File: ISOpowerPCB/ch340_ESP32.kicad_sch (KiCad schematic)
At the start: 8 parts

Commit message: significant changes
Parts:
- added SW?: EN, symbol 000_Switches_Immo:pushbutton_tactile_2pin_SMD
- added SW?: BOOT, symbol 000_Switches_Immo:pushbutton_tactile_2pin_SMD
- R? (x2): value Resistor_0805 -> 10k
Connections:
- net ESP_EN: now also SW?.1
- net ESP_IO0: now also SW?.1
- net GND: now also SW?.2, SW?.2
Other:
- note removed: "USB power routed to its own bus, to allow potential for USB power to be used for powering microcontrollers during programming, but avoid case where user inadvertently tries to power entire 5v BUS from USB rail"
- moved on the sheet: C?, J?, Q?, R?, U?

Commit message: Updated as per discussions 26/01/22
# Change Notes

04/02/2022
As per discussion 26/01/22
1. Changed per channel 5v MOSFET switches to MOSFET control of DC/DC module on/off pin - due to failure of MOSFET switching during testing.
2. Added 5v buck converter for independent MCU_5V power bus.
	- Ensured all 5v MCU hardware is powered from common MCU_5V bus.
3. Removed circuit from NC pins on DC/DC modules.
4. Changed ESP32 USB interface to CH340
5. Changed MCU serial logic level converters from MOSFET to IC - TXS0102DCT
	- TODO: OE pin now requires low signal untill DC/DC supply is stable - Does it? Can it just be tied to 5v bus with a large capacitor? Does it need MCU to hold pin low untill 5V_BUS is stable?
6. Removed redundent 3V3_IN to power distribution page.
	- Rechecked all sheets for redundent pins, it won't impact drawing traces, but it will impact readability.
7. Added Mechanical layer as hirarchical sheet.
8. Moved voltage monitoring circuits to hirarchical sheet
9. Added voltage monitoring with TL431DBZ to 12V_BUS
10. Automatic shutoff circuit removed, as this would prevent the DC/DC module from powering on. Instead moved to AtMega328p digital inputs
and microcontroller will control shutdown of DC/DC supply if out of spec voltage detected.
		- This is a severe limitation compared to the specification, and this also does not prevent damage to devices on 5V_BUS if voltage is pulled high, for example to 12v due to user error.
		- TODO: Add independent overvoltage protection to 5V_BUS? 		[Zener Diode Overvoltage Protection - Sparkfun](https://www.rs-online.com/designspark/how-does-zener-diode-do-overvoltage-protection-in-circuit#:~:text=In%20order%20to%20protect%20the,flow%20in%20the%20reverse%20direction).
11. Changed logic level conversion for 12v outputs to 12v drive circuit. [12v drive circuit](https://forum.arduino.cc/t/easiest-way-of-driving-amplifying-from-5v-to-12v/123290)
12. Added proto pin connections for ESP MCU.
13. Changed 20v Zener in reverse vol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
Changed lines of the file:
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@@
     (effects (font (size 1.27 1.27)) (justify left))
   )
-  (hierarchical_label "GND" (shape bidirectional) (at 25.4 24.13 180)
+  (hierarchical_label "GND" (shape passive) (at 25.4 24.13 180)
     (effects (font (size 1.27 1.27)) (justify right))
   )

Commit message: messing around with libraries
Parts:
- C28, C29: renamed from C?; symbol 000_Capacitor_film_immo:cap_film_0805 -> 000_Capacitor_FIlm_Immo:cap_film_0805
- gave numbers to parts that had none: 8
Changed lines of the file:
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@@
     (effects (font (size 1.27 1.27)) (justify left))
   )
-  (symbol (lib_id "000_Capacitor_film_immo:cap_film_0805") (at 127 66.04 270) (mirror x) (unit 1)
-    (in_bom yes) (on_board yes)
-    (property "Reference" "C?" (id 0) (at 129.54 64.77 90))
+  (symbol (lib_id "000_Capacitor_FIlm_Immo:cap_film_0805") (at 127 66.04 270) (mirror x) (unit 1)
+    (in_bom yes) (on_board yes)
+    (property "Reference" "C28" (id 0) (at 129.54 64.77 90))
     (property "Value" "100n" (id 1) (at 123.19 64.77 90))
     (property "Footprint" "Capacitor_SMD:C_0805_2012Metric_Pad1.18x1.45mm_HandSolder" (id 2) (at 116.84 64.77 0)
@@
   (symbol (lib_id "power:GND") (at 199.39 92.71 0) (mirror y) (unit 1)
     (in_bom yes) (on_board yes) (fields_autoplaced)
-    (property "Reference" "#PWR?" (id 0) (at 199.39 99.06 0)
+    (property "Reference" "#PWR086" (id 0) (at 199.39 99.06 0)
       (effects (font (size 1.27 1.27)) hide)
     )
@@
   (symbol (lib_id "power:GND") (at 116.84 72.39 0) (mirror y) (unit 1)
     (in_bom yes) (on_board yes) (fields_autoplaced)
-    (property "Reference" "#PWR?" (id 0) (at 116.84 78.74 0)
+    (property "Reference" "#PWR084" (id 0) (at 116.84 78.74 0)
       (effects (font (size 1.27 1.27)) hide)
     )
@@
   (symbol (lib_id "Interface_USB:CH340C") (at 135.89 87.63 0) (unit 1)
     (in_bom yes) (on_board yes) (fields_autoplaced)
-    (property "Reference" "U?" (id 0) (at 135.3694 102.87 0)
+    (property "Reference" "U14" (id 0) (at 135.3694 102.87 0)
       (effects (font (size 1.27 1.27)) (justify right))
     )
@@
   (symbol (lib_id "power:GND") (at 90.17 113.03 0) (mirror y) (unit 1)
     (in_bom yes) (on_board yes) (fields_autoplaced)
-    (property "Reference" "#PWR?" (id 0) (at 90.17 119.38 0)
+    (property "Reference" "#PWR083" (id 0) (at 90.17 119.38 0)
       (effects (font (size 1.27 1.27)) hide)
     )
@@
     (pin "1")
   )
-  (symbol (lib_id "000_Capacitor_film_immo:cap_film_0805") (at 127 71.12 270) (mirror x) (unit 1)
-    (in_bom yes) (on_board yes)
-    (property "Reference" "C?" (id 0) (at 129.54 69.85 90))
+  (symbol (lib_id "000_Capacitor_FIlm_Immo:cap_film_0805") (at 127 71.12 270) (mirror x) (unit 1)
+    (in_bom yes) (on_board yes)
+    (property "Reference" "C29" (id 0) (at 129.54 69.85 90))
     (property "Value" "100n" (id 1) (at 123.19 69.85 90))
     (property "Footprint" "Capacitor_SMD:C_0805_2012Metric_Pad1.18x1.45mm_HandSolder" (id 2) (at 116.84 69.85 0)
@@
   (symbol (lib_id "power:GND") (at 36.83 24.13 90) (unit 1)
     (in_bom yes) (on_board yes) (fields_autoplaced)
-    (property "Reference" "#PWR?" (id 0) (at 43.18 24.13 0)
+    (property "Reference" "#PWR082" (id 0) (at 43.18 24.13 0)
       (effects (font (size 1.27 1.27)) hide)
     )
@@
   (symbol (lib_id "Transistor_BJT:BC817") (at 182.88 88.9 0) (unit 1)
     (in_bom yes) (on_board yes) (fields_autoplaced)
-    (property "Reference" "Q?" (id 0) (at 187.96 87.6299 0)
+    (property "Reference" "Q19" (id 0) (at 187.96 87.6299 0)
       (effects (font (size 1.27 1.27)) (justify left))
     )
@@
   (symbol (lib_id "000_Switches_Immo:pushbutton_tactile_2pin_SMD") (at 196.85 119.38 270) (unit 1)
     (in_bom yes) (on_board yes) (fields_autoplaced)
-    (property "Reference" "SW?" (id 0) (at 203.2 118.0799 90)
+    (property "Reference" "SW3" (id 0) (at 203.2 118.0799 90)
       (effects (font (size 1.27 1.27)) (justify left))
     )
@@
   (symbol (lib_id "power:GND") (at 199.39 125.73 0) (mirror y) (unit 1)
     (in_bom yes) (on_board yes) (fields_autoplaced)
-    (property "Reference" "#PWR?" (id 0) (at 199.39 132.08 0)
+    (property "Reference" "#PWR087" (id 0) (at 199.39 132.08 0)
       (effects (font (size 1.27 1.27)) hide)
     )
@@
   (symbol (lib_id "000_Resistors_Immo:Resistor_0805") (at 168.91 88.9 90) (unit 1)
     (in_bom yes) (on_board yes)
-    (property "Reference" "R?" (id 0) (at 168.91 86.36 90))
+    (property "Reference" "R25" (id 0) (at 168.91 86.36 90))
     (property "Value" "10k" (id 1) (at 168.91 91.44 90))
     (property "Footprint" "Resistor_SMD:R_0805_2012Metric_Pad1.20x1.40mm_HandSolder" (id 2) (at 168.91 90.678 90)
@@
   (symbol (lib_id "000_Resistors_Immo:Resistor_0805") (at 168.91 104.14 90) (unit 1)
     (in_bom yes) (on_board yes)
-    (property "Reference" "R?" (id 0) (at 168.91 101.6 90))
+    (property "Reference" "R26" (id 0) (at 168.91 101.6 90))
     (property "Value" "10k" (id 1) (at 168.91 106.68 90))
     (property "Footprint" "Resistor_SMD:R_0805_2012Metric_Pad1.20x1.40mm_HandSolder" (id 2) (at 168.91 105.918 90)
@@
   (symbol (lib_id "Connector:USB_B_Mini") (at 90.17 85.09 0) (unit 1)
     (in_bom yes) (on_board yes) (fields_autoplaced)
-    (property "Reference" "J?" (id 0) (at 83.82 83.8199 0)
+    (property "Reference" "J20" (id 0) (at 83.82 83.8199 0)
       (effects (font (size 1.27 1.27)) (justify right))
     )
@@
   (symbol (lib_id "000_Switches_Immo:pushbutton_tactile_2pin_SMD") (at 196.85 86.36 270) (unit 1)
     (in_bom yes) (on_board yes) (fields_autoplaced)
-    (property "Reference" "SW?" (id 0) (at 203.2 85.0599 90)
+    (property "Reference" "SW2" (id 0) (at 203.2 85.0599 90)
       (effects (font (size 1.27 1.27)) (justify left))
     )
@@
   (symbol (lib_id "power:GND") (at 135.89 109.22 0) (mirror y) (unit 1)
     (in_bom yes) (on_board yes) (fields_autoplaced)
-    (property "Reference" "#PWR?" (id 0) (at 135.89 115.57 0)
+    (property "Reference" "#PWR085" (id 0) (at 135.89 115.57 0)
       (effects (font (size 1.27 1.27)) hide)
     )
@@
   (symbol (lib_id "Transistor_BJT:BC817") (at 182.88 104.14 0) (mirror x) (unit 1)
     (in_bom yes) (on_board yes) (fields_autoplaced)
-    (property "Reference" "Q?" (id 0) (at 187.96 102.8699 0)
-      (effects (font (size 1.27 1.27)) (justify left))
-    )
+    (property "Reference" "Q20" (id 0) (at 187.96 102.8699 0)
+      (effects (font (size 1.27 1.27)) (justify left))
+    )

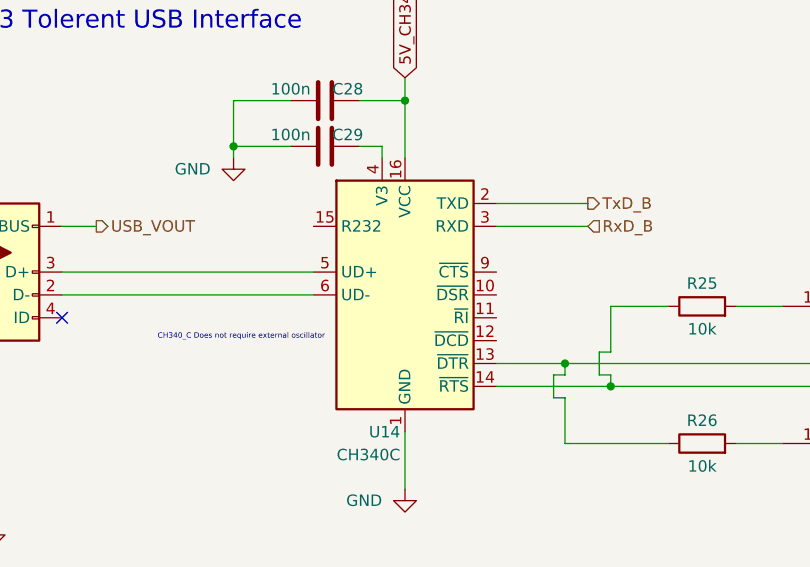
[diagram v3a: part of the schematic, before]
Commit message: adding logic for fault indication
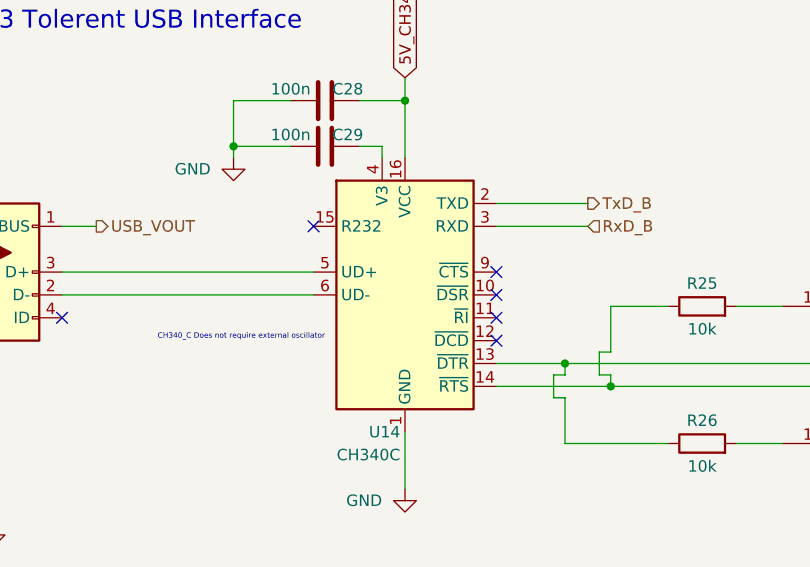
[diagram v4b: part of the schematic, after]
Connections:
- no-connect marks 1 -> 6
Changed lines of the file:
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@@
   )
   (no_connect (at 97.79 90.17))
+  (no_connect (at 146.05 90.17))
+  (no_connect (at 125.73 80.01))
+  (no_connect (at 146.05 85.09))
+  (no_connect (at 146.05 87.63))
+  (no_connect (at 146.05 92.71))
   (wire (pts (xy 87.63 99.06) (xy 90.17 99.06))
     (stroke (width 0) (type default) (color 0 0 0 0))

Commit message: fixed most electrical rules check violations
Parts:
- C28, C29: symbol 000_Capacitor_FIlm_Immo:cap_film_0805 -> 000_Capacitor_Film_Immo:cap_film_0805
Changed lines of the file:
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@@
     (effects (font (size 1.27 1.27)) (justify left))
   )
-  (symbol (lib_id "000_Capacitor_FIlm_Immo:cap_film_0805") (at 127 66.04 270) (mirror x) (unit 1)
+  (symbol (lib_id "000_Capacitor_Film_Immo:cap_film_0805") (at 127 66.04 270) (mirror x) (unit 1)
     (in_bom yes) (on_board yes)
     (property "Reference" "C28" (id 0) (at 129.54 64.77 90))
@@
     (pin "1")
   )
-  (symbol (lib_id "000_Capacitor_FIlm_Immo:cap_film_0805") (at 127 71.12 270) (mirror x) (unit 1)
+  (symbol (lib_id "000_Capacitor_Film_Immo:cap_film_0805") (at 127 71.12 270) (mirror x) (unit 1)
     (in_bom yes) (on_board yes)
     (property "Reference" "C29" (id 0) (at 129.54 69.85 90))

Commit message: added documentation for component selection
Completed footprint association & added documentation re Netclasses. Need to update netclasses in schematic settings before moving to PCB layout.
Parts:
- J20: footprint (none) -> Connector_USB:USB_Mini-B_Lumberg_2486_01_Horizontal
- SW2, SW3: footprint (none) -> Button_Switch_SMD:SW_SPST_EVQPE1
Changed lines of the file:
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@@
       (effects (font (size 1.27 1.27)) (justify left))
     )
-    (property "Footprint" "" (id 2) (at 204.47 119.38 0)
+    (property "Footprint" "Button_Switch_SMD:SW_SPST_EVQPE1" (id 2) (at 204.47 119.38 0)
       (effects (font (size 1.27 1.27)) hide)
     )
@@
       (effects (font (size 1.27 1.27)) (justify right))
     )
-    (property "Footprint" "" (id 2) (at 93.98 86.36 0)
+    (property "Footprint" "Connector_USB:USB_Mini-B_Lumberg_2486_01_Horizontal" (id 2) (at 93.98 86.36 0)
       (effects (font (size 1.27 1.27)) hide)
     )
@@
       (effects (font (size 1.27 1.27)) (justify left))
     )
-    (property "Footprint" "" (id 2) (at 204.47 86.36 0)
+    (property "Footprint" "Button_Switch_SMD:SW_SPST_EVQPE1" (id 2) (at 204.47 86.36 0)
       (effects (font (size 1.27 1.27)) hide)
     )
